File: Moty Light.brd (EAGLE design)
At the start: 58.5 x 48.2 mm, 21 parts, among them Q1 C1815, Q2 C1815

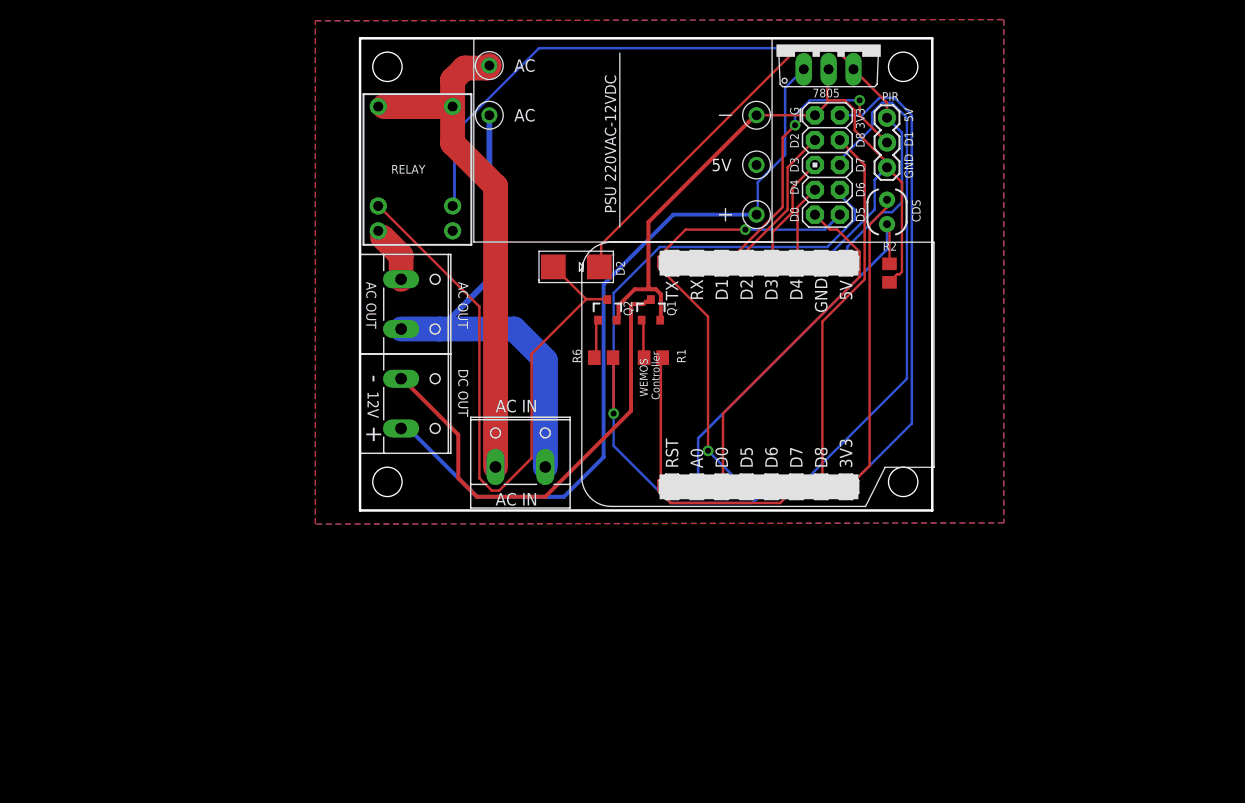
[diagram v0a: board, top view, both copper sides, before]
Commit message: Update to new version to match size of new box
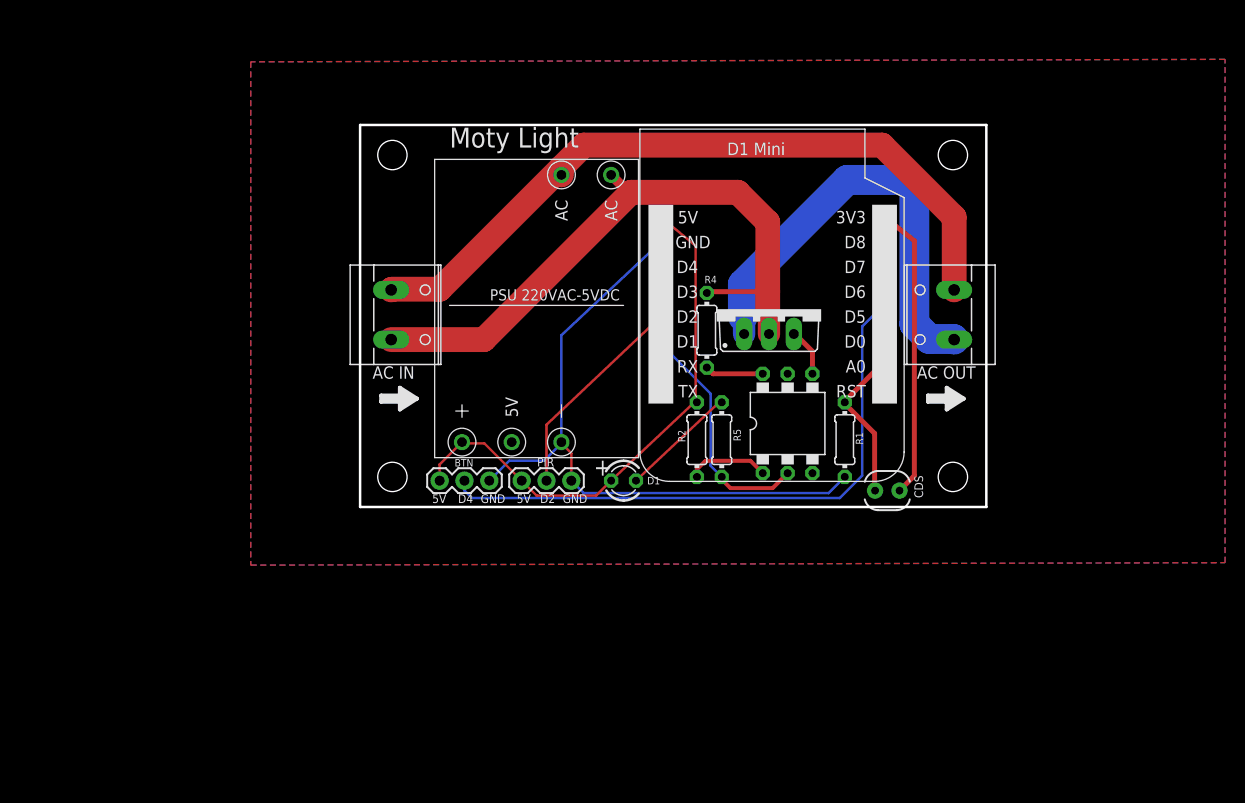
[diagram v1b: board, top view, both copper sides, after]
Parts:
- removed 12V: (no value), con-wago-508:W237-132
- removed 7805: 7805_, linear:TO220V
- removed D2: (no value), adafruit:SMADIODE
- removed JP2: (no value), SparkFun-Connectors:AVR_ICSP
- removed Q1, Q2: C1815, SparkFun-DiscreteSemi:SOT23-3
- removed R6: 1K, rcl:R0805
- added BUTTON: BTN, SparkFun-Connectors:1X03
- added D1: (no value), led:LED3MM
- added OK1: MOC3041, optocoupler:DIL06B
- added R4: 180, rcl:0204/7
- added R5: 330, rcl:0204/7
- added T1: BTA16, triac:TO220BV
- added U$2: (no value), dicons:ICON_ARROW-S
- R1: value 1K -> 10K; device rcl:R0805 -> rcl:0204/7
- R2: value 10K -> 330; device rcl:R0805 -> rcl:0204/7
- U$1: value RELAY -> (none); device My Eagle Lib:MINIATURE_RELAY_JRC_21F -> dicons:ICON_ARROW-S
- U$10: value WEMOSLOCKED -> WEMOSNORMAL; device My Eagle Lib:WEMOS_LOCKED -> My Eagle Lib:WEMOS
- moved AC_OUT 55.3 mm to (85.0, 51.0), turned to 90 degrees
- moved PIR 45.4 mm to (46.5, 34.0), turned to 180 degrees
- moved R3 28.6 mm to (78.9, 33.0), turned to 180 degrees
- moved U$10 27.8 mm to (78.5, 61.0), turned to 180 degrees
- moved R2 26.0 mm to (59.3, 38.2), turned to 270 degrees
- moved U$1 23.7 mm to (29.0, 42.4)
- moved R1 21.3 mm to (74.4, 38.2), turned to 90 degrees
- moved AC 19.5 mm to (28.7, 51.0), turned to 270 degrees
- moved U$3 18.9 mm to (42.9, 51.9), turned to 270 degrees
- moved U$17 18.5 mm to (43.7, 46.0)
- moved U$8 10.3 mm to (85.5, 67.3)
- moved U$9 9.03 mm to (28.2, 67.3)
- moved U$7 5.11 mm to (85.5, 34.4)
- moved U$6 0.72 mm to (28.2, 34.4)
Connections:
- removed net 12V: 12V.2, 7805.1, U$3.J2.3
- removed net N$1: 12V.1, Q1.3
- removed net N$3: D2.A, Q2.3, U$1.COIL2
- removed net N$4: Q2.1, R6.2
- removed net N$7: Q1.1, R1.2
- removed net N$8: AC_OUT.1, U$1.NO
- new net N$10: OK1.1, R2.2
- new net N$14: OK1.6, R4.1
- new net N$23: AC_OUT.1, T1.T1
- new net N$28: D1.K, R5.1
- new net N$9: OK1.4, T1.G
- net 3V3: no longer JP2.2
- net 5V: now also BUTTON.3, D1.A, R2.1, U$3.J2.3; no longer 7805.3, D2.C, U$1.COIL1
- net A0: now also R1.2; no longer R2.2
- net AC_L: now also AC.2, R4.2, T1.T2; no longer AC.1, U$1.COM1, U$1.COM2
- net AC_N: now also AC.1; no longer AC.2
- net D0: no longer JP2.9
- net D1: now also OK1.2, R5.2; no longer PIR.2
- net D2: now also PIR.2; no longer JP2.3
- net D3: no longer JP2.5
- net D4: no longer JP2.7
- net D5: now also BUTTON.2; no longer JP2.10
- net D6: no longer JP2.8, R6.1
- net D7: no longer JP2.6, R1.1
- net D8: no longer JP2.4
- net GND: now also BUTTON.1, R1.1; no longer 7805.2, JP2.1, Q1.2, Q2.2, R2.1
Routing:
- net D7: track 83.0 -> 0.00 mm
- net 12V: track 78.4 -> 0.00 mm
- net D6: track 72.1 -> 0.00 mm, vias 1 -> 0
- net N$3: track 64.8 -> 0.00 mm
- net 5V: track 115.8 -> 55.6 mm
- net 3V3: track 81.1 -> 30.0 mm
- net N$1: track 47.9 -> 0.00 mm
- net N$23: track 0.00 -> 45.9 mm
- net D8: track 38.3 -> 0.00 mm
- net D0: track 35.9 -> 0.00 mm
- net AC_N: track 50.9 -> 74.9 mm
- net A0: track 39.2 -> 16.7 mm
- net AC_L: track 52.8 -> 66.5 mm
- net D5: track 47.8 -> 61.5 mm, vias 2 -> 0
- net N$28: track 0.00 -> 12.0 mm
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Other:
- board size 58.5 x 48.2 mm -> 64 x 39 mm
- board text added: "PSU 220VAC-5VDC"
- board text removed: "-"
- board text removed: "12V"
- board text removed: "3V3"
- board text removed: "D0"
- board text removed: "D1"
- board text removed: "D3"
- board text removed: "D5"
- board text removed: "D6"
- board text removed: "D7"
- board text removed: "D8"
- board text removed: "DC OUT"
- board text removed: "G"
- board text removed: "PSU 220VAC-12VDC"

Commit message: Update design to use SSR and fit in a box and update code to support view status and config via web
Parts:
- BUTTON: value BTN -> Button
- moved BUTTON 4.07 mm to (42.2, 34.3)
- moved D1 3.56 mm to (55.4, 34.0)
- moved PIR 3.31 mm to (49.8, 34.3)
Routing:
- net GND: track 67.4 -> 61.7 mm
- net D5: track 61.5 -> 56.9 mm
- net N$28: track 12.0 -> 10.3 mm
- net D2: track 21.8 -> 22.8 mm
- net 5V: track 55.6 -> 55.0 mm
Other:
- board size 64 x 39 mm -> 64 x 40 mm
- board text added: "D5"
- board text added: "PWR LED"
- board text removed: "D4"

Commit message: Update to version 0.2
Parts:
- removed AC_OUT: (no value), con-wago-508:W237-132
- removed BUTTON: Button, SparkFun-Connectors:1X03
- removed OK1: MOC3041, optocoupler:DIL06B
- removed T1: BTA16, triac:TO220BV
- removed U$1, U$2: (no value), dicons:ICON_ARROW-S
- removed U$6: (no value), penn-engineering:KFH-M3
- added AC1, AC2: (no value), con-wago-508:W237-132
- added BTN2: BTN2, SparkFun-Connectors:1X03
- added BUTTON1: BTN1, SparkFun-Connectors:1X03
- added C1, C1815: C1815, SparkFun-DiscreteSemi:SOT23-3
- added C2: 47uF/16V, SparkFun-Capacitors:CPOL-RADIAL-10UF-25V
- added C3: 102pF, SparkFun-Capacitors:CPOL-RADIAL-10UF-25V
- added D2: (no value), adafruit:SMADIODE
- added N1: N4148, adafruit:SOD-123
- added N4148: (no value), adafruit:SOD-123
- added PWR_LED: PWR, adafruit:LED3MM
- added R6, R8, R9: 1K, rcl:R0805
- added R7: 4.7K, rcl:R0805
- added RELAY1, RELAY2: ZNS5106, relay:ZN5
- added RELAY_LED1: RELAY1, adafruit:LED3MM
- added RELAY_LED2: Relay2, adafruit:LED3MM
- D1: device led:LED3MM -> adafruit:SMADIODE
- R1: device rcl:0204/7 -> rcl:R0805
- R2, R5: value 330 -> 1K; device rcl:0204/7 -> rcl:R0805
- R4: value 180 -> 4.7K; device rcl:0204/7 -> rcl:R0805
- moved U$7 40.8 mm to (52.2, 10.8)
- moved R4 29.8 mm to (56.9, 19.8)
- moved U$9 25.2 mm to (4.06, 59.9)
- moved AC 25.2 mm to (8.38, 36.1)
- moved R3 22.9 mm to (71.2, 54.6), turned to 0 degrees
- moved PIR 22.1 mm to (71.6, 37.3), turned to 270 degrees
- moved D1 22.0 mm to (38.6, 19.8), turned to 90 degrees
- moved R2 21.5 mm to (48.3, 19.8), turned to 90 degrees
- moved R5 20.6 mm to (52.6, 19.8), turned to 90 degrees
- moved U$17 19.8 mm to (23.9, 45.0)
- moved U$3 19.2 mm to (23.7, 52.1), turned to 0 degrees
- moved R1 17.4 mm to (61.2, 26.9), turned to 270 degrees
- moved U$8 15.3 mm to (72.0, 59.9)
- moved U$10 14.0 mm to (66.5, 53.6)
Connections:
- removed net AC_L: AC.2, R4.2, T1.T2, U$3.J1.1
- removed net AC_N: AC.1, AC_OUT.2, U$3.J1.2
- removed net N$14: OK1.6, R4.1
- removed net N$23: AC_OUT.1, T1.T1
- removed net N$28: D1.K, R5.1
- new net HOT: AC.2, RELAY1.11, RELAY2.11, U$3.J1.1
- new net N$1: C1815.3, D2.A, RELAY1.A2, RELAY_LED1.K
- new net N$3: N4148.C, R6.1
- new net N$4: R8.2, RELAY_LED1.A
- new net N$5: C1.3, D1.A, RELAY2.A2, RELAY_LED2.K
- new net N$6: C1.1, R2.2, R4.2
- new net N$7: C1815.1, R6.2, R7.2
- new net N$8: N1.C, R2.1
- new net NC1: RELAY1.12
- new net NC2: RELAY2.12
- new net NEUTRAL: AC.1, AC1.2, AC2.2, U$3.J1.2
- new net NO1: AC1.1, RELAY1.14
- new net NO2: AC2.1, RELAY2.14
- net 5V: now also BTN2.3, BUTTON1.3, C2.1, C3.1, D1.C, D2.C, R5.1, R8.1, R9.1, RELAY1.A1, RELAY2.A1; no longer BUTTON.3, D1.A, R2.1
- net D1: now also N4148.A; no longer OK1.2, R5.2
- net D2: now also N1.A; no longer PIR.2
- net D5: now also BUTTON1.2; no longer BUTTON.2
- net D6: now also BTN2.2
- net D7: now also PIR.2
- net GND: now also BTN2.1, BUTTON1.1, C1.2, C1815.2, C2.2, C3.2, PWR_LED.K, R4.1, R7.1; no longer BUTTON.1
- net N$10: now also PWR_LED.A, R9.2; no longer OK1.1, R2.2
- net N$9: now also R5.2, RELAY_LED2.A; no longer OK1.4, T1.G
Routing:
- net 5V: track 55.0 -> 212.6 mm, vias 0 -> 5
- net AC_N: track 74.9 -> 0.00 mm
- net AC_L: track 66.5 -> 0.00 mm
- net GND: track 61.7 -> 122.9 mm
- net HOT: track 0.00 -> 58.0 mm
- net NEUTRAL: track 0.00 -> 52.4 mm
- net N$1: track 0.00 -> 51.3 mm
- net N$5: track 0.00 -> 50.8 mm, vias 0 -> 1
- net N$23: track 45.9 -> 0.00 mm
- net D6: track 0.00 -> 35.1 mm
- net A0: track 16.7 -> 43.8 mm
- net 3V3: track 30.0 -> 3.97 mm
- net D5: track 56.9 -> 31.1 mm
- net NO2: track 0.00 -> 25.1 mm
- net D7: track 0.00 -> 23.4 mm
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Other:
- board size 64 x 40 mm -> 75.2 x 55.5 mm
- board text added: "D6"
- board text added: "D7"
- board text added: "Moty Light V0.2"
- board text added: "RELAY1"
- board text added: "RELAY2"
- board text removed: "+"
- board text removed: "AC OUT"
- board text removed: "D2"
- board text removed: "Moty Light"
- board text removed: "PWR LED"

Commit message: Update design to version 0.3
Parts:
- removed C1, C1815: C1815, SparkFun-DiscreteSemi:SOT23-3
- removed U$9: (no value), penn-engineering:KFH-M3
- added Q1, Q2: C1815, SparkFun-DiscreteSemi:SOT23-3
- RELAY_LED1: value RELAY1 -> Relay1
- moved R5 16.9 mm to (36.6, 14.5)
- moved R8 12.5 mm to (36.6, 31.2)
- moved RELAY_LED1 11.4 mm to (36.3, 25.7), turned to 270 degrees
- moved U$7 10.9 mm to (41.3, 10.8)
- moved RELAY_LED2 7.96 mm to (36.3, 19.6), turned to 90 degrees
- moved U$10 7.37 mm to (59.2, 53.8)
- moved R3 6.18 mm to (65.2, 55.6)
- moved U$17 5.34 mm to (18.5, 44.7)
- moved U$3 5.34 mm to (18.4, 51.8)
- moved BUTTON1 4.83 mm to (68.3, 14.0)
- moved BTN2 4.83 mm to (57.4, 13.7)
- moved C2 4.83 mm to (66.8, 48.3)
- moved C3 4.83 mm to (66.8, 42.9)
- moved PIR 4.83 mm to (66.8, 37.3)
- moved N1 3.81 mm to (47.8, 21.6)
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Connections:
- net GND: now also Q1.2, Q2.2; no longer C1.2, C1815.2
- net N$1: now also Q1.3; no longer C1815.3
- net N$5: now also Q2.3; no longer C1.3
- net N$6: now also Q2.1; no longer C1.1
- net N$7: now also Q1.1; no longer C1815.1
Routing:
- net N$5: track 50.8 -> 34.9 mm, vias 1 -> 0
- net N$9: track 16.8 -> 2.92 mm
- net A0: track 43.8 -> 30.4 mm
- net N$4: track 15.4 -> 3.98 mm, vias 1 -> 0
- net N$6: track 22.0 -> 13.3 mm, vias 2 -> 0
- net 5V: track 212.6 -> 204.6 mm, vias 5 -> 1
- net D7: track 23.4 -> 17.4 mm
- net N$3: track 8.75 -> 4.37 mm
- net GND: track 122.9 -> 119.8 mm
- net D2: track 24.2 -> 27.1 mm, vias 0 -> 1
- net N$7: track 14.4 -> 11.9 mm
- net D1: track 14.1 -> 16.6 mm
- net N$1: track 51.3 -> 49.4 mm, vias 0 -> 2
- net 3V3: track 3.97 -> 5.56 mm
- net N$10: track 6.98 -> 5.45 mm
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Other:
- board size 75.2 x 55.5 mm -> 70.3 x 55.5 mm
- board text added: "Moty Light V0.3"
- board text removed: "Moty Light V0.2"

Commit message: Update design to version 1.0
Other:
- board text added: "Moty Light v1.0"
- board text removed: "Moty Light V0.3"
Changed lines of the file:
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@@
 <text x="26.289" y="56.134" size="1.143" layer="25" font="vector" ratio="15" rot="R180">PSU 220VAC-5VDC</text>
 <text x="25.908" y="50.165" size="1.524" layer="25" font="vector" ratio="15" rot="R180">HIGH VOLTAGE</text>
-<text x="50.038" y="8.382" size="1.651" layer="25" font="vector" ratio="20" rot="SR0">Moty Light V0.3</text>
+<text x="50.038" y="8.382" size="1.651" layer="25" font="vector" ratio="20" rot="SR0">Moty Light v1.0</text>
 <text x="51.562" y="11.176" size="0.889" layer="25" font="vector" ratio="15">5V</text>
 <text x="68.707" y="54.61" size="0.889" layer="25" font="vector" ratio="15" rot="SR90">CDS</text>
